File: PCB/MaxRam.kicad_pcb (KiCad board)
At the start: 2 copper layers, 74.9 x 40.6 mm, 15 parts, among them J1 CONN_01X14, J2 CONN_01X04, J3 CONN_02X05, J4 CONN_01X03, J5 CONN_01X03, J6 CONN_01X14, J7 CONN_01X02, U1 AS6C4008-55SIN, U2 SST39SF040, U3 ATF1502PLCC44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

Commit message: Update PCB Still getting used to KiCad / PCB Design
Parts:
- moved J4 35.1 mm to (153.7, 110.5)
- moved C4 7.62 mm to (181.6, 106.7), turned to 270 degrees
- moved C1 7.50 mm to (127.0, 101.6), turned to 180 degrees
- moved C3 7.50 mm to (147.2, 101.6), turned to 180 degrees
- moved J5 2.54 mm to (153.7, 101.6)
- moved J2 1.27 mm to (153.7, 128.5)
- moved J7 1.27 mm to (153.7, 134.6)
- moved U2 1.27 mm to (115.6, 101.6)
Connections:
- C1 pad 1: +5V -> Net-(C1-Pad1)
- C1 pad 2: Net-(C1-Pad2) -> GND
- C2 pad 2: Net-(C1-Pad2) -> GND
- C3 pad 2: Net-(C1-Pad2) -> GND
- C4 pad 2: Net-(C1-Pad2) -> GND
- J1 pad 14: Net-(C1-Pad2) -> GND
- J3 pad 10: Net-(C1-Pad2) -> GND
- J3 pad 2: Net-(C1-Pad2) -> GND
- J4 pad 1: Net-(J4-Pad1) -> /We
- J5 pad 2: /S18 -> /PIN30
- J6 pad 1: Net-(J6-Pad1) -> +5V
- J7 pad 2: Net-(C1-Pad2) -> GND
- U1 pad 16: Net-(C1-Pad2) -> GND
- U1 pad 24: /Romsel -> Net-(J6-Pad7)
- U1 pad 29: Net-(J4-Pad1) -> /We
- U1 pad 32: Net-(U1-Pad32) -> Net-(C1-Pad1)
- U2 pad 24: /Romsel -> Net-(J6-Pad7)
- U2 pad 30: /S18 -> /PIN30
- U2 pad 31: Net-(J4-Pad1) -> /We
- U3 pad 10: Net-(C1-Pad2) -> GND
- U3 pad 2: /Romsel -> Net-(J6-Pad7)
- U3 pad 22: Net-(C1-Pad2) -> GND
- U3 pad 30: Net-(C1-Pad2) -> GND
- U3 pad 40: Net-(U2-Pad22) -> Net-(U3-Pad40)
- U3 pad 42: Net-(C1-Pad2) -> GND
- U3 pad 44: /We -> /Romsel
- U4 pad 1: Net-(U1-Pad32) -> Net-(C1-Pad1)
- U4 pad 3: Net-(C1-Pad2) -> GND
- U4 pad 7: Net-(C1-Pad2) -> GND
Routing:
- net GND: track 0.00 -> 125.2 mm
- net /D4: track 0.00 -> 86.5 mm, vias 0 -> 2
- net /D5: track 0.00 -> 81.4 mm, vias 0 -> 2
- net /S15: track 0.00 -> 58.0 mm
- net /D3: track 0.00 -> 56.7 mm
- net /D7: track 0.00 -> 56.7 mm
- net /D6: track 0.00 -> 56.7 mm
- net +5V: track 0.00 -> 42.8 mm
- net /We: track 0.00 -> 29.1 mm
- net /S14: track 0.00 -> 29.0 mm
- net /TDI: track 0.00 -> 26.0 mm
- net Net-(C1-Pad1): track 0.00 -> 24.3 mm
- net /D1: track 0.00 -> 23.9 mm
- net /A0: track 0.00 -> 23.9 mm
- net /A4: track 0.00 -> 23.9 mm
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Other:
- net class Power added: clearance 0.2, trace_width 0.508, via_dia 0.6, via_drill 0.4

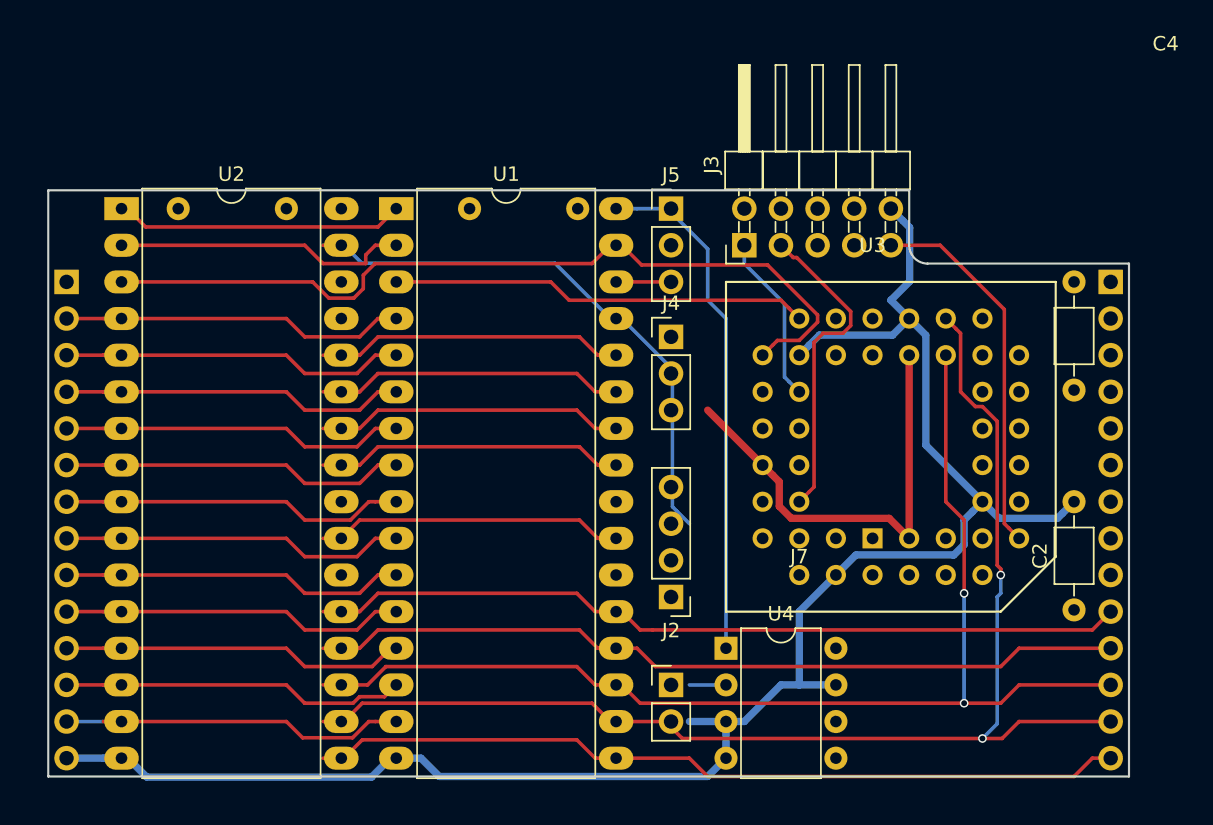
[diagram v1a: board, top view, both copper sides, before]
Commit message: Add PCB with CPLD at rats nest
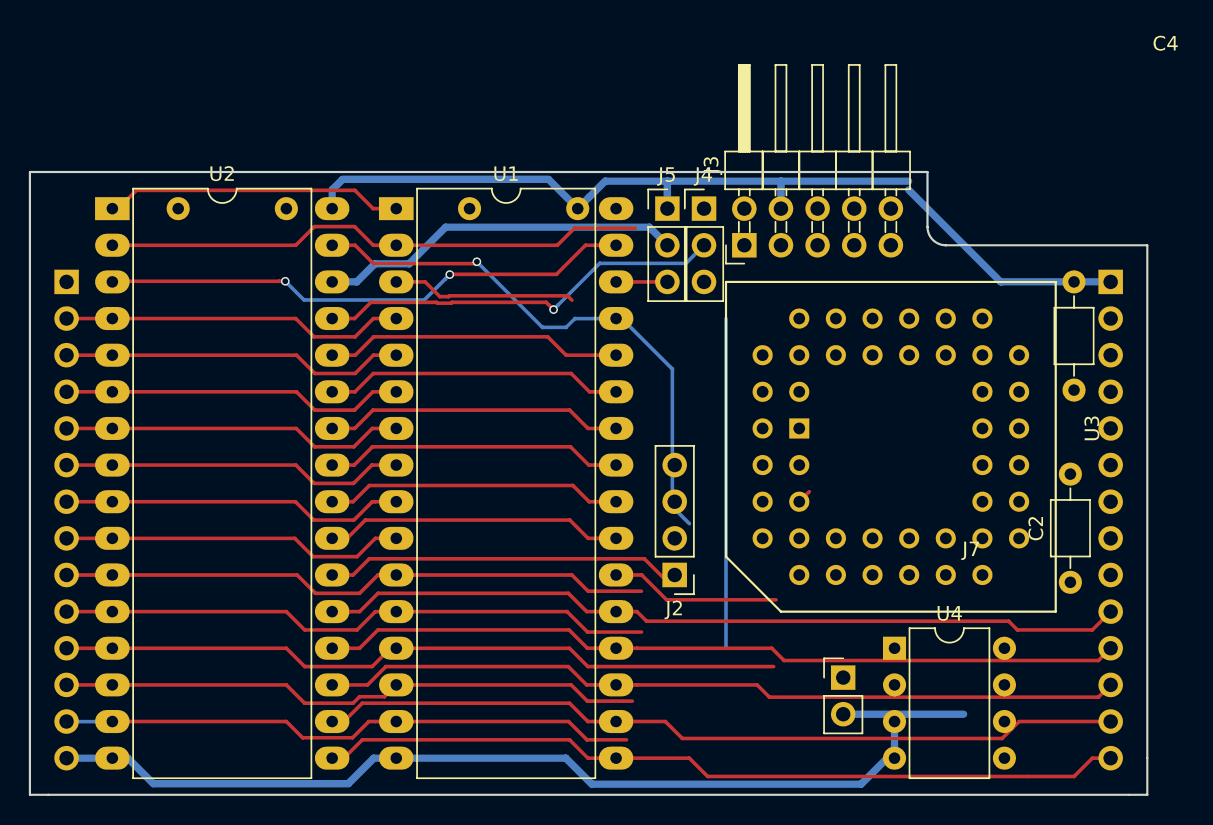
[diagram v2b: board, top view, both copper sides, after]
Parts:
- moved J7 11.9 mm to (165.6, 134.1)
- moved U4 11.7 mm to (169.2, 132.1)
- moved J4 9.18 mm to (156.0, 101.6)
- moved C2 1.93 mm to (181.4, 127.5)
- moved J2 1.55 mm to (153.9, 127.0)
- moved U2 0.63 mm to (114.9, 101.6)
- moved J5 0.25 mm to (153.4, 101.6)
- turned U3 to 0 degrees
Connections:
- net Net-(J6-Pad7) renamed /nOE
- J4 pad 3: Net-(J4-Pad3) -> /S14
- U2 pad 22: Net-(U2-Pad22) -> /FLASH_CE
- U2 pad 32: VCC -> +5V
- U3 pad 33: Net-(U3-Pad33) -> /S17
- U3 pad 34: Net-(U3-Pad34) -> /S18
- U3 pad 40: Net-(U3-Pad40) -> /FLASH_CE
- U4 pad 8: VCC -> +5V
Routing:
- net GND: track 125.2 -> 71.5 mm
- net /D4: track 86.5 -> 56.6 mm, vias 2 -> 0
- net /D0: track 23.9 -> 50.6 mm
- net /TDI: track 26.0 -> 0.00 mm
- net /PIN30: track 0.00 -> 25.7 mm
- net /D5: track 81.4 -> 56.4 mm, vias 2 -> 0
- net Net-(C1-Pad1): track 24.3 -> 0.00 mm
- net (no net): track 0.00 -> 22.9 mm
- net /CLK: track 0.00 -> 22.5 mm
- net /S15: track 58.0 -> 36.8 mm, vias 0 -> 2
- net /TDO: track 22.2 -> 0.99 mm
- net +5V: track 42.8 -> 63.7 mm
- net /nOE: track 0.00 -> 20.6 mm
- net Net-(J4-Pad2): track 11.2 -> 29.2 mm, vias 0 -> 1
- net /A0: track 23.9 -> 41.5 mm
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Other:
- board size 74.9 x 40.6 mm -> 77.5 x 43.2 mm

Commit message: PCB all routed
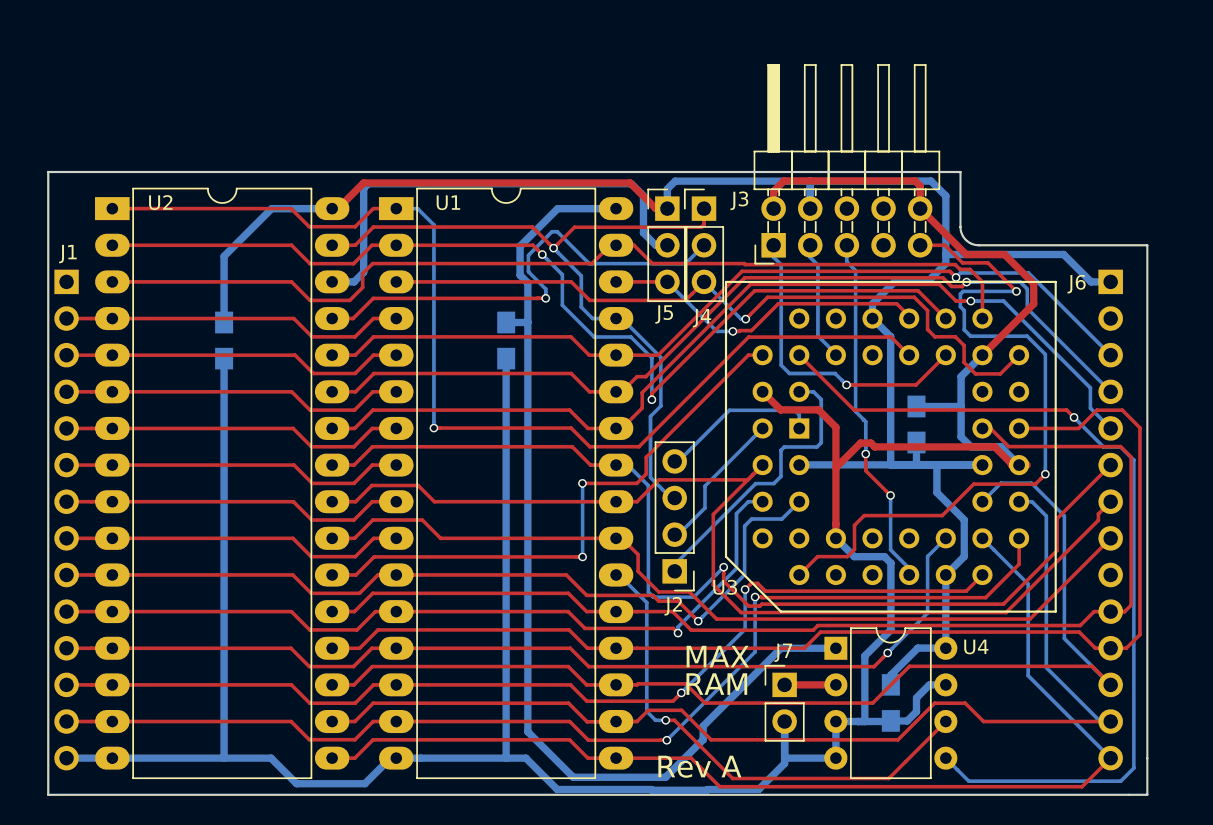
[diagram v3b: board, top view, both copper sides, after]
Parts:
- C1, C3: footprint Capacitors_ThroughHole:C_Axial_L3.8mm_D2.6mm_P7.50mm_Horizontal -> Capacitors_SMD:C_0805_HandSoldering
- C2, C4: footprint Capacitors_ThroughHole:C_Axial_L3.8mm_D2.6mm_P7.50mm_Horizontal -> Capacitors_SMD:C_0805_HandSoldering; moved to B.Cu
- moved C2 61.0 mm to (122.7, 110.7), turned to 270 degrees
- moved C4 31.8 mm to (168.9, 135.9)
- moved C3 27.9 mm to (170.7, 116.6), turned to 90 degrees
- moved C1 17.8 mm to (142.2, 110.7), turned to 270 degrees
- moved J7 4.10 mm to (161.5, 134.6)
- moved U4 4.06 mm to (165.1, 132.1)
- moved J3 2.03 mm to (160.8, 104.1)
- moved J2 0.25 mm to (153.9, 126.7)
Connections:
- net Net-(C1-Pad1) renamed /VBAT
- net Net-(J7-Pad1) renamed /BAT
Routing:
- net GND: track 71.5 -> 219.6 mm
- net +5V: track 63.7 -> 138.1 mm
- net /VBAT: track 0.00 -> 70.1 mm
- net Net-(U3-Pad41): track 0.00 -> 61.6 mm, vias 0 -> 1
- net /S18: track 20.7 -> 75.0 mm, vias 0 -> 1
- net /nOE: track 20.6 -> 73.3 mm
- net /A11: track 21.4 -> 71.7 mm, vias 0 -> 1
- net /TDI: track 0.00 -> 50.1 mm, vias 0 -> 2
- net /A9: track 21.4 -> 65.4 mm, vias 0 -> 1
- net /A8: track 21.4 -> 63.2 mm, vias 0 -> 1
- net /A10: track 21.4 -> 61.0 mm
- net /A13: track 21.4 -> 60.7 mm, vias 0 -> 1
- net /FLASH_CE: track 1.45 -> 39.8 mm, vias 0 -> 2
- net /S14: track 12.8 -> 50.1 mm, vias 0 -> 1
- net /D2: track 40.3 -> 76.7 mm, vias 0 -> 2
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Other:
- board size 77.5 x 43.2 mm -> 76.2 x 43.2 mm
- board text added: "MAX"
- board text added: "RAM"
- board text added: "Rev A"

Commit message: PCB now has a ground plane (copper pour)
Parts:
- moved C1 9.91 mm to (146.1, 101.6), turned to 180 degrees
- moved C2 9.81 mm to (126.2, 101.6), turned to 180 degrees
- moved C4 2.94 mm to (170.4, 133.3)
- moved C3 2.35 mm to (168.9, 118.1), turned to 0 degrees
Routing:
- net +5V: track 138.1 -> 117.5 mm, vias 0 -> 2
- net /VBAT: track 70.1 -> 50.6 mm, vias 0 -> 1
- net Net-(U3-Pad41): track 61.6 -> 42.9 mm, vias 1 -> 4
- net GND: track 219.6 -> 236.8 mm
- net /TDI: track 50.1 -> 42.2 mm
- net /TMS: track 24.7 -> 30.4 mm, vias 2 -> 1
- net /D4: track 77.2 -> 81.3 mm
- net /D3: track 76.2 -> 80.3 mm
- net /S18: track 75.0 -> 78.3 mm
- net /D7: track 79.7 -> 83.0 mm, vias 0 -> 1
- net /D6: track 82.8 -> 85.9 mm, vias 0 -> 3
- net Net-(J4-Pad2): track 34.0 -> 31.1 mm
- net /D0: track 68.5 -> 70.9 mm
- net /D5: track 78.0 -> 80.4 mm
- net Net-(U1-Pad22): track 34.8 -> 36.9 mm
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- added copper zone on F.Cu, net +5V
- added copper zone on B.Cu, net GND
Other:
- net class Default: clearance 0.2 -> 0.2032; trace_width 0.25 -> 0.2032
- net class Power: clearance 0.2 -> 0.2032
- rule trace_clearance: 0.2 -> 0.2032
- rule trace_min: 0.2 -> 0.2032
- board text added: "MAX RAM"

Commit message: Latest PCB including plane and pin swapped CPLD, still messy
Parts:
- added G***: LOGO, OPENHARDWARE:OSHWLOGO0.3IN, F.Cu at (174.2, 133.6)
- added J8: CONN_01X05, Pin_Headers:Pin_Header_Straight_1x05_Pitch2.54mm, F.Cu at (180.3, 124.5)
- J1: moved to F.Cu
- moved J2 25.8 mm to (170.2, 106.7), turned to 270 degrees
- moved J3 0.76 mm to (160.0, 104.1)
- turned J1 to 0 degrees
- turned U3 to 180 degrees
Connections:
- net Net-(J4-Pad2) renamed /PIN29
- net Net-(U1-Pad22) renamed /RAM_nCE
- J2 pad 1: /CLK -> Net-(J2-Pad1)
- J2 pad 2: /Romsel -> Net-(J2-Pad2)
- J2 pad 3: /We -> /WE_in
- J2 pad 4: /CsIn -> Net-(J2-Pad4)
- J4 pad 1: /We -> /nWE
- J6 pad 7: /nOE -> /OE_IN
- U1 pad 28: /A13 -> /S13
- U1 pad 29: /We -> /nWE
- U1 pad 4: /A12 -> /S12
- U2 pad 22: /FLASH_CE -> /FLASH_nCE
- U2 pad 28: /A13 -> /S13
- U2 pad 31: /We -> /nWE
- U2 pad 4: /A12 -> /S12
- U3 pad 11: Net-(U3-Pad11) -> /WE_in
- U3 pad 12: Net-(U3-Pad12) -> /S15
- U3 pad 14: Net-(U3-Pad14) -> /S18
- U3 pad 16: /D0 -> /nWE
- U3 pad 17: /D1 -> /S14
- U3 pad 18: /D2 -> /S16
- U3 pad 19: /D3 -> /S17
- U3 pad 2: /nOE -> /OE_IN
- U3 pad 20: /D4 -> /S12
- U3 pad 21: /D5 -> /S13
- U3 pad 24: /D6 -> /nOE
- U3 pad 25: /D7 -> /A12
- U3 pad 26: Net-(U3-Pad26) -> /FLASH_nCE
- U3 pad 27: Net-(U3-Pad27) -> /A1
- U3 pad 28: /S14 -> /A0
- U3 pad 29: /S15 -> /D0
- U3 pad 31: /S16 -> /D1
- U3 pad 33: /S17 -> /D2
- U3 pad 34: /S18 -> Net-(U3-Pad34)
- U3 pad 36: Net-(U3-Pad36) -> /D3
- U3 pad 37: Net-(U3-Pad37) -> /D4
- U3 pad 39: Net-(U3-Pad39) -> /D5
- U3 pad 4: /A0 -> /Z2
- U3 pad 40: /FLASH_CE -> /D7
- U3 pad 41: Net-(U3-Pad41) -> /D6
- U3 pad 5: /A1 -> /Z1
- U3 pad 6: Net-(U3-Pad6) -> /A13
- U3 pad 8: Net-(U3-Pad8) -> Net-(J2-Pad1)
- U3 pad 9: Net-(U3-Pad9) -> Net-(J2-Pad2)
- U4 pad 5: Net-(U3-Pad41) -> Net-(U3-Pad34)
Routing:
- net /nWE: track 0.00 -> 56.7 mm
- net /A13: track 60.7 -> 6.35 mm
- net /We: track 50.0 -> 0.00 mm, vias 1 -> 0
- net /S12: track 0.00 -> 48.2 mm
- net Net-(U3-Pad41): track 42.9 -> 0.00 mm, vias 4 -> 0
- net /A12: track 23.9 -> 64.7 mm, vias 0 -> 3
- net /nOE: track 75.3 -> 34.9 mm
- net /FLASH_CE: track 39.8 -> 0.00 mm, vias 2 -> 0
- net /S13: track 0.00 -> 36.2 mm
- net /TDI: track 42.2 -> 7.76 mm, vias 2 -> 0
- net /FLASH_nCE: track 0.00 -> 32.9 mm, vias 0 -> 1
- net /TDO: track 8.36 -> 39.5 mm, vias 0 -> 2
- net /TMS: track 30.4 -> 6.13 mm, vias 1 -> 0
- net Net-(U3-Pad34): track 0.00 -> 20.6 mm
- net /OE_IN: track 0.00 -> 20.5 mm
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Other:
- board text added: "1"
- board text added: "SPFMDB"

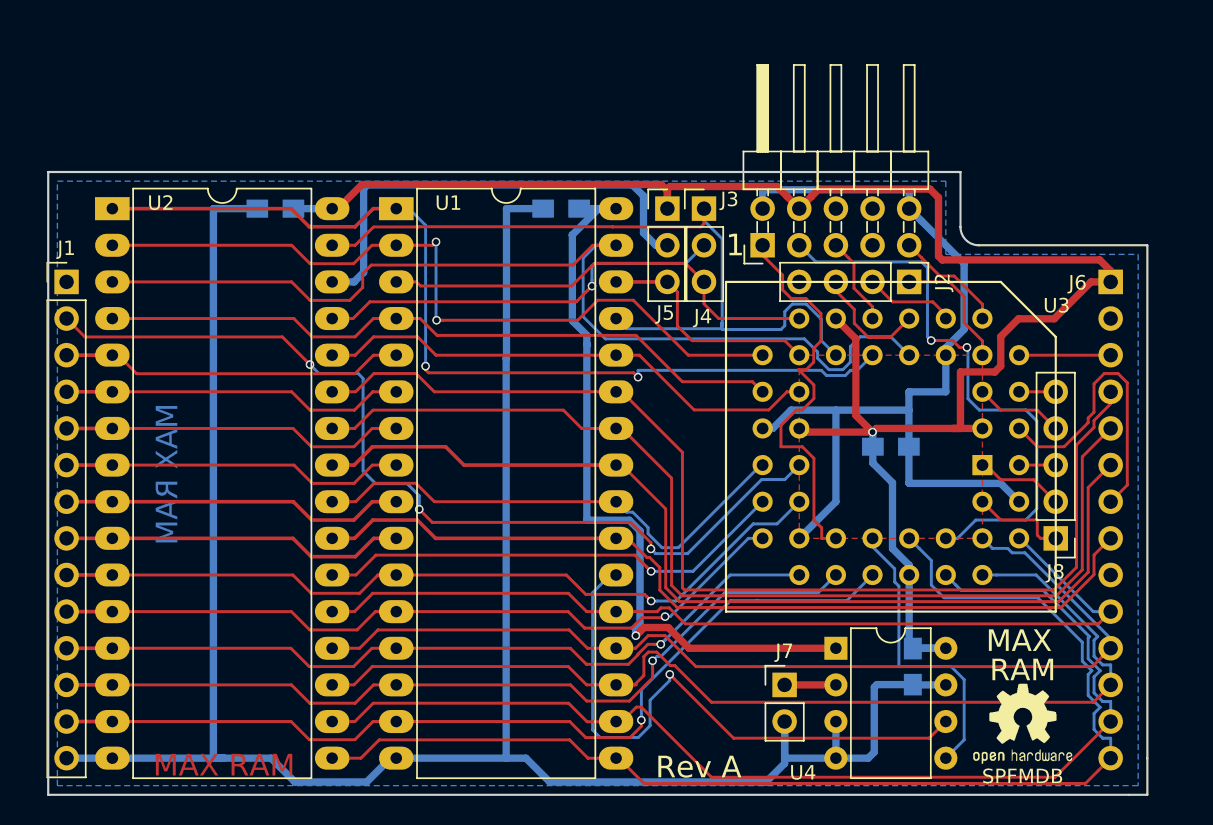
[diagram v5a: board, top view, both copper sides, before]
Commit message: Work in progress, about to fix overlapping parts
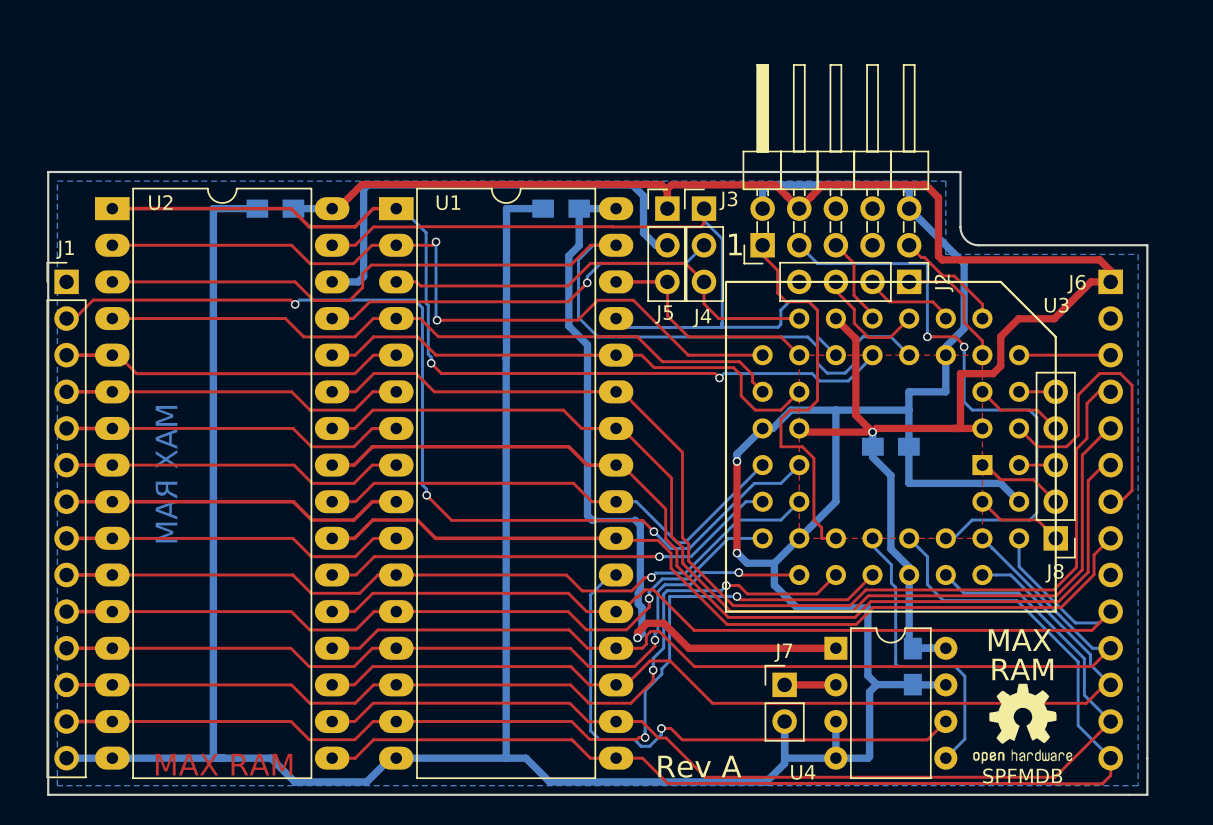
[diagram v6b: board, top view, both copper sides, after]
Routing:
- net GND: track 224.0 -> 253.2 mm, vias 0 -> 2
- net /A12: track 64.7 -> 68.5 mm
- net /D2: track 63.6 -> 67.1 mm, vias 1 -> 2
- net /RAM_nCE: track 41.8 -> 38.5 mm
- net /D7: track 65.0 -> 68.2 mm
- net /D1: track 59.2 -> 62.2 mm, vias 1 -> 2
- net /D5: track 73.5 -> 70.6 mm
- net /D4: track 78.7 -> 76.0 mm
- net /D0: track 54.9 -> 57.2 mm, vias 1 -> 2
- net /S15: track 70.6 -> 71.9 mm
- net /OE_IN: track 20.5 -> 21.5 mm
- net /FLASH_nCE: track 32.9 -> 31.9 mm
- net /S13: track 36.2 -> 37.0 mm
- net /S18: track 65.7 -> 64.8 mm
- net /TDO: track 39.5 -> 40.3 mm
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
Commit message: Latest design. PLCC now on it's own, a bit more tweaking yet.
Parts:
- J1: moved to B.Cu
- J2: value CONN_01X04 -> CONN_01X03; footprint Pin_Headers:Pin_Header_Straight_1x04_Pitch2.54mm -> Pin_Headers:Pin_Header_Straight_1x03_Pitch2.54mm
- J4, J5: value CONN_01X03 -> GS3; footprint Pin_Headers:Pin_Header_Straight_1x03_Pitch2.54mm -> Connectors:GS3; moved to B.Cu
- moved J5 26.6 mm to (127.3, 106.2), turned to 180 degrees
- moved J4 18.1 mm to (138.2, 104.9), turned to 180 degrees
- moved J2 11.4 mm to (180.3, 111.8), turned to 180 degrees
- moved J3 2.54 mm to (157.5, 104.1)
- moved C3 2.54 mm to (166.4, 118.1)
- moved U3 2.54 mm to (166.4, 118.1)
- turned J1 to 180 degrees
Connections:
- net Net-(J2-Pad1) renamed /Z3
- net Net-(J2-Pad2) renamed /Z4
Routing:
- net /PIN30: track 33.2 -> 3.13 mm
- net /S17: track 16.4 -> 35.6 mm, vias 0 -> 1
- net /PIN29: track 29.0 -> 14.7 mm, vias 1 -> 0
- net /A12: track 68.5 -> 61.0 mm, vias 3 -> 4
- net /nWE: track 56.7 -> 50.0 mm, vias 0 -> 2
- net /WE_in: track 8.32 -> 13.8 mm, vias 0 -> 2
- net /nOE: track 34.3 -> 29.4 mm
- net /Z4: track 6.41 -> 11.2 mm, vias 0 -> 2
- net /A10: track 62.0 -> 66.2 mm
- net /S18: track 64.8 -> 68.5 mm
- net /A13: track 6.35 -> 9.93 mm
- net /OE_IN: track 21.5 -> 24.1 mm
- net /CLK: track 6.14 -> 8.69 mm
- net /Z2: track 2.54 -> 5.08 mm
- net /Romsel: track 2.54 -> 5.08 mm
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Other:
- outline, holes or cut-outs redrawn

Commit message: All fixed up version
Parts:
- removed J2: CONN_01X03, Pin_Headers:Pin_Header_Straight_1x03_Pitch2.54mm
- J8: value CONN_01X05 -> CONN_01X08; footprint Pin_Headers:Pin_Header_Straight_1x05_Pitch2.54mm -> Pin_Headers:Pin_Header_Straight_1x08_Pitch2.54mm
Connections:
- U3 pad 11: /WE_in -> /CS_in
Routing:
- net /CS_in: track 0.00 -> 13.8 mm, vias 0 -> 2
- net /WE_in: track 13.8 -> 0.00 mm, vias 2 -> 0
- net +5V: track 127.2 -> 128.7 mm
- net /D7: track 70.7 -> 69.2 mm
- net /A0: track 50.6 -> 51.8 mm
- net /D2: track 64.7 -> 63.5 mm
- net /VBAT: track 50.9 -> 49.9 mm
- net /TCK: track 27.6 -> 26.8 mm
- net /A11: track 72.5 -> 71.8 mm
- net /D1: track 60.5 -> 59.8 mm
- net /A9: track 76.0 -> 75.4 mm
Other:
- board text added: "+"
- board text added: "-"
